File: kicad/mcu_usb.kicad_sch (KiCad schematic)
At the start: 45 parts, among them J4 USB-A host, SW2 BOOT, U10 RP2354A, U11 SRV05-4, U12 SY6280AAC, U6 SRV05-4, Y1 12MHz

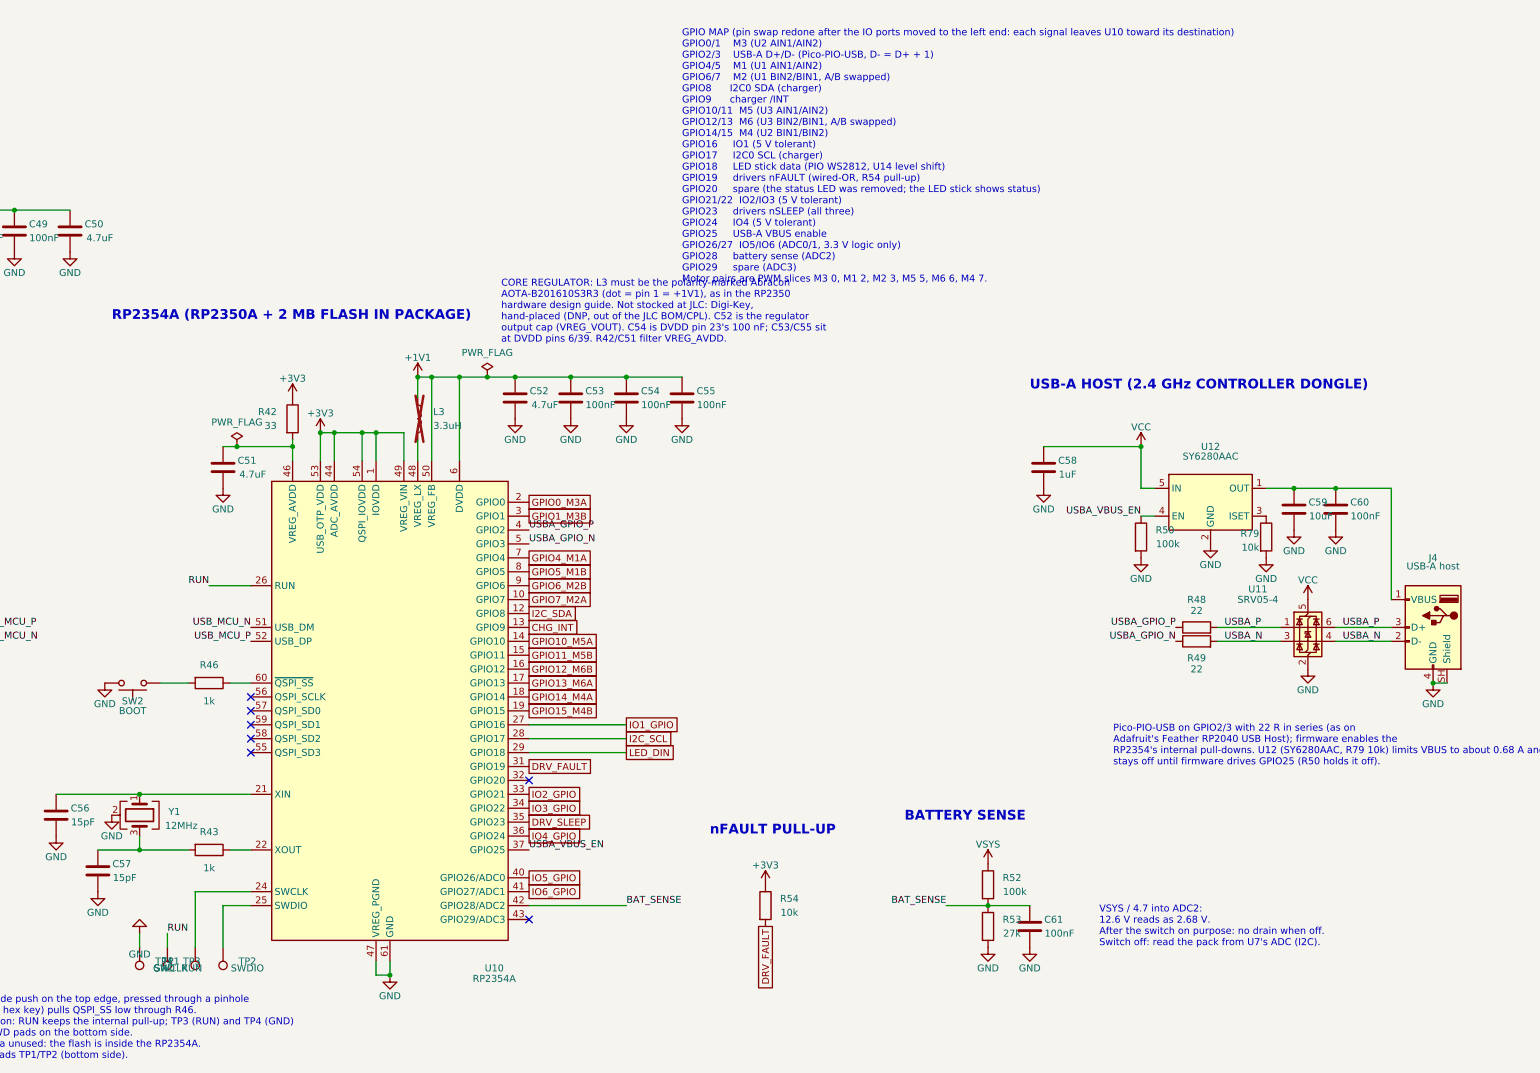
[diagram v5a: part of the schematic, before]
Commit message: Fix the buck inductor, soft-start VSYS and limit motor current
Circuit (goosebrain.py, PARTS.md, schematic):
- L1 is a Coilcraft XAL5030-222 (Isat 9.2 A, the AP64500's max current
  limit). The old CR4030 saturated at about 3.1 A.
- VSYS soft start and clamp: C71 gate-drain and C72 gate-source on Q1,
  R40 27k, R41 10k, and an SMF14A TVS (D4) on VSYS.
- Each DRV8848 chops at about 1.33 A per bridge: 0.15 R sense resistors
  on AISEN/BISEN and a 15k/10k VREF divider from VINT, so six stalled
  motors can't reach the protector's OCD1 trip.
- U4 gets a second 10 uF (C73) and a 100 nF (C74) at VIN.
- Stock swaps after a full JLC stock check: D4 to the Littelfuse SMF14A,
  the sense resistors to YAGEO RL1206FR-7W0R15L (500 mW).

Board:
- New parts placed and routed. The sense resistors are close to their
  pins; U2's B-side runs on F.Cu only.
- 22 more VSYS vias (Q1 drain to the In3 plane, each driver's VM caps,
  both ends of U4's VIN jumper).
- C63 (AVDD) and C68 (SRP-SRN) moved next to the BQ7791501.
- Goose logo on the back silkscreen.
- Review 63: DRC 0 errors, unrouted 0, parity clean, no new DRC types.

tools/fab.py adds per-package rotation offsets read off JLC's placement
preview. The README covers them, the D4 polarity check, the corrected
current limits and the low-stock parts.

Co-Authored-By: Claude Opus 5.5 <noreply@anthropic.com>
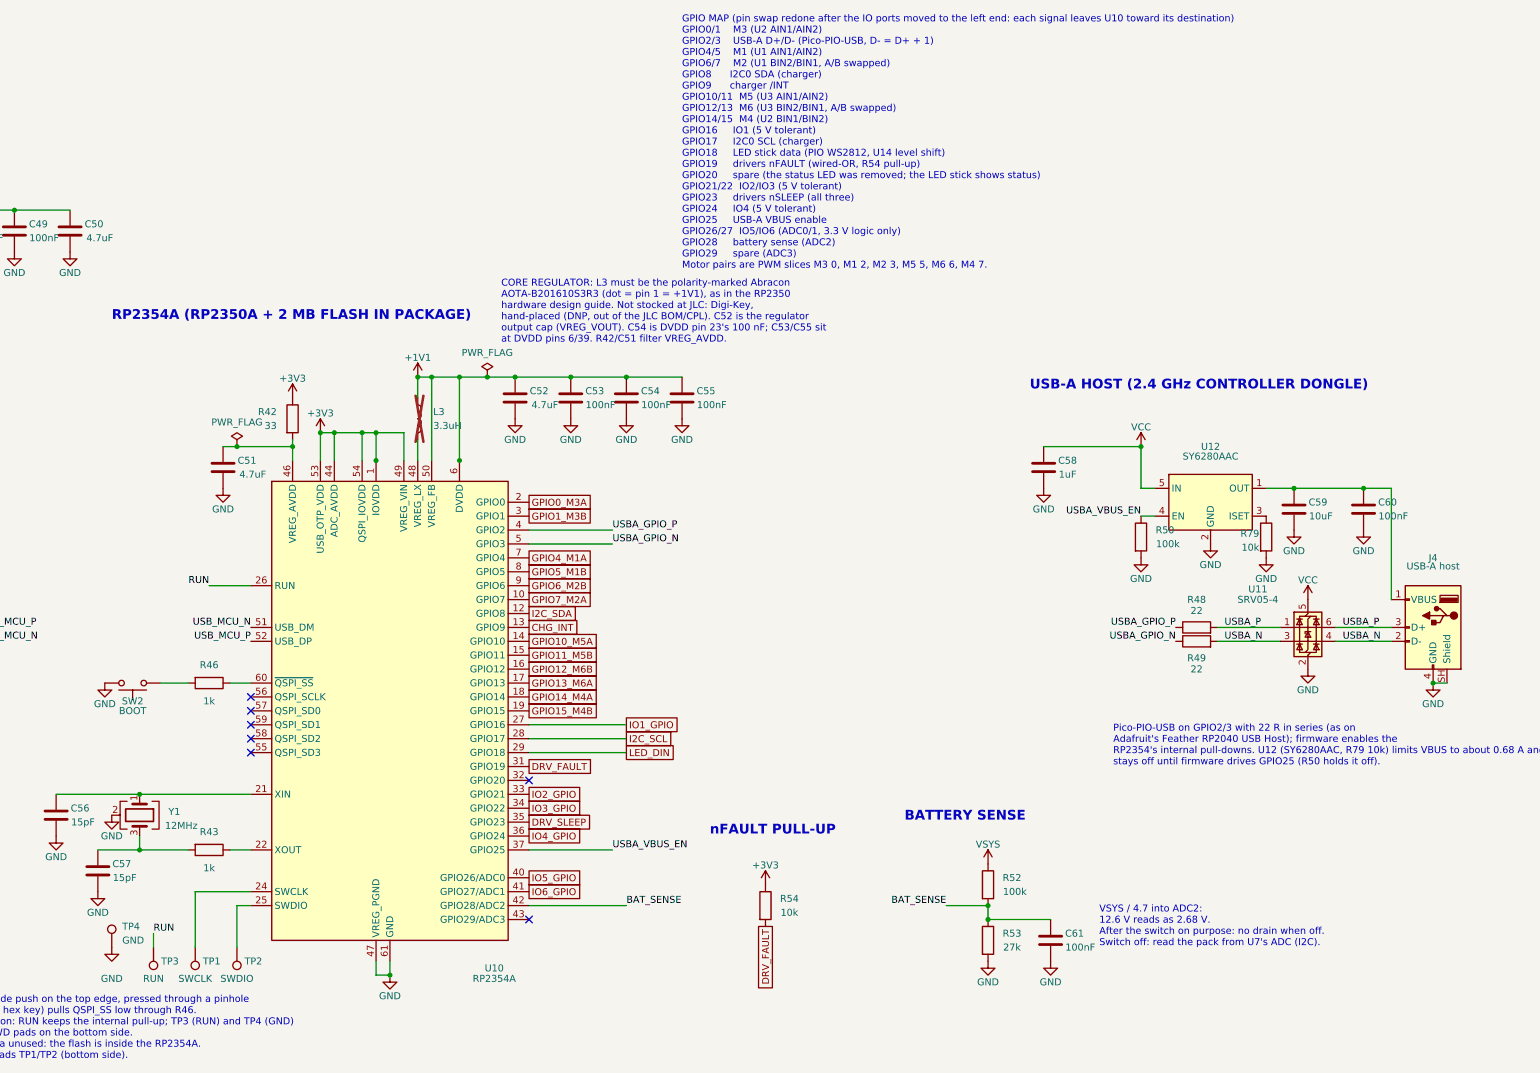
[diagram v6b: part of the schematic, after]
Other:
- moved on the sheet: C60, C61, R53, TP2, TP3

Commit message: Split into brain + smart pack, and support 2S packs
Brain/pack split: charging, protection and the fuse move off the brain
into a separate smart pack board (kicad-pack/goosepack), with its own
USB-C charging port. The brain drops to 4 layers, loses the charger,
PD sink, protector and SY6280, and swaps the DRV8848s for DRV8871s.

2S support on the brain:
- DRV8871 -> DRV8251A (same HSOP-8 footprint, 4.5-48 V VM). Shared VREF
  divider R107/R108/C81 from +3V3 (2.53 V) and 1.18k IPROPI resistors
  keep the 1.36 A limit.
- Q1 gate divider 27k/10k -> 47k/4.7k for -5.1 V drive at an empty 2S
  pack; C71 4.7n -> 10n to keep the ~70 us soft start.

New 2S pack variant (kicad-pack-2s/goosepack2s): BQ25798 PROG 8.2k
(2S, 750 kHz), ILIM R33 18k (~0.42 A charge), ABLIC S-8252AAH protector
in place of the BQ7791501, two HY2213-BB3A balancers with AO3400A and
47R 2512 bleed resistors, 3-pin XH balance header, R94 4.7k for trip
recovery. fab.py builds it with --board pack2s.

Several new parts still need LCSC numbers; fab.py flags each one.

Co-Authored-By: Claude Opus 5.5 <noreply@anthropic.com>
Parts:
- removed C58: 1uF, Capacitor_SMD:C_0402_1005Metric, symbol Device:C
- removed C60: 100nF, Capacitor_SMD:C_0402_1005Metric, symbol Device:C
- removed R50: 100k, Resistor_SMD:R_0402_1005Metric, symbol Device:R
- removed R54, R79: 10k, Resistor_SMD:R_0402_1005Metric, symbol Device:R
- removed U12: SY6280AAC, Package_TO_SOT_SMD:SOT-23-5, symbol hexyhustle:SY6280AAC
- added F2: 0.5A hold, Fuse:Fuse_1206_3216Metric, symbol Device:Polyfuse
- SW2: now not fitted
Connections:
- net VCC: now also F2.1
- net at C59.1, J4.1 (VBUS): now also F2.2
- net CHG_INT: no longer names the net of U10.13 (GPIO9)
- net DRV_FAULT: no longer names the net of U10.31 (GPIO19)
- net DRV_SLEEP: no longer names the net of U10.35 (GPIO23)
- net I2C_SCL: no longer names the net of U10.28 (GPIO17)
- net I2C_SDA: no longer names the net of U10.12 (GPIO8)
- net USBA_VBUS_EN: no longer names the net of U10.37 (GPIO25)
- no-connect marks 7 -> 13
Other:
- note added: "GPIO MAP GPIO0/1 M3 (U2 IN1/IN2) GPIO2/3 USB-A D+/D- (Pico-PIO-USB, D- = D+ + 1) GPIO4/5 M1 (U1 IN1/IN2) GPIO6/7 M2 (U15 IN2/IN1, A/B swapped) GPIO8, 9 spare (no-connect; were I2C SDA and charger /INT) GPIO10/11 M5 (U3 IN1/IN2) GPIO12/13 M6 (U17 IN2/IN1, A/B swapped) GPIO14/15 M4 (U16 IN1/IN2) GPIO16 IO1 (5 V tolerant) GPIO17 spare (no-connect; was I2C SCL) GPIO18 LED stick data (PIO WS2812, U14 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"
- note added: "USB-A VBUS: F2 PTC from VCC (0.5 A hold, 1 A trip, 16 V, 1206, hand-placed); C59 10 uF at the port. Always powered: no enable GPIO. Pico-PIO-USB on GPIO2/3 with 22 R in series."
- note added: "VSYS / 4.7 into ADC2: 12.6 V reads as 2.68 V. After the switch on purpose: no drain when off. The pack cuts off at 2.8 V/cell (8.4 V) in hardware."
- note removed: "GPIO MAP (pin swap redone after the IO ports moved to the left end: each signal leaves U10 toward its destination) GPIO0/1 M3 (U2 AIN1/AIN2) GPIO2/3 USB-A D+/D- (Pico-PIO-USB, D- = D+ + 1) GPIO4/5 M1 (U1 AIN1/AIN2) GPIO6/7 M2 (U1 BIN2/BIN1, A/B swapped) GPIO8 I2C0 SDA (charger) GPIO9 charger /INT GPIO10/11 M5 (U3 AIN1/AIN2) GPIO12/13 M6 (U3 BIN2/BIN1, A/B swapped) GPIO14/15 M4 (U2 BIN1/BIN2) GPIO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"
- note removed: "Pico-PIO-USB on GPIO2/3 with 22 R in series (as on Adafruit's Feather RP2040 USB Host); firmware enables the RP2354's internal pull-downs. U12 (SY6280AAC, R79 10k) limits VBUS to about 0.68 A and stays off until firmware drives GPIO25 (R50 holds it off)."
- note removed: "VSYS / 4.7 into ADC2: 12.6 V reads as 2.68 V. After the switch on purpose: no drain when off. Switch off: read the pack from U7's ADC (I2C)."
- note removed: "nFAULT PULL-UP"
